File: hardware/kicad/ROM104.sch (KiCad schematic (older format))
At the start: 43 parts, among them J1 Screw_Terminal_01x06, J2 Screw_Terminal_01x06, J3 Screw_Terminal_01x06, J4 CAN, K1 SPDT_RELAY, K2 SPDT_RELAY, K3 SPDT_RELAY, K4 SPDT_RELAY, K5 SPDT_RELAY, K6 SPDT_RELAY, SW1 HEX_ENCODER, SW2 BUS, SW3 HEX_ENCODER, U1 L293D, U2 74HC595, U3 L293D, U4 L293D, U5 MCP2551-I-P, U6 TMR_2411, U7 Teensy_3.2

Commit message: New PCB layout
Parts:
- removed D1, D2, D3, D4, D5, D6, D7, D8: D_Small, Diode_THT:D_DO-34_SOD68_P2.54mm_Vertical_AnodeUp, symbol Device:D_Small
- removed SW1, SW3: HEX_ENCODER, PDJR-connectors:FR01-SR16P-ST, symbol pdjr:HEX_ENCODER
- added C1: 100n, Capacitor_THT:C_Rect_L4.6mm_W3.0mm_P2.50mm_MKS02_FKP02, symbol Device:C
- added SW1: INSTANCE, Package_DIP:DIP-16_W7.62mm, symbol Switch:SW_DIP_x08
- renumbered D9 to D1, D10 to D2, D11 to D3, D12 to D4, D13 to D5, D14 to D6, D15 to D7, D16 to D8, U3 to U2, U2 to U3
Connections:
- net labels added: ADDR_4, ADDR_5, ADDR_6, ADDR_7
- net labels removed: ADDR_HI, ADDR_LO
- no-connect marks 13 -> 11
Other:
- moved on the sheet: D1, D2, D3, D4, D5, D6, D7, D8, RN1, SW2, U3

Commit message: Add PRG switch
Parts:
- added SW3: PRG, Button_Switch_THT:SW_PUSH_6mm, symbol Switch:SW_Push
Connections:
- net labels added: PRG
- wire segments 290 -> 292
- no-connect marks 11 -> 10
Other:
- moved on the sheet: SW1, SW2
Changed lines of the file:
@@
 L power:GND #PWR02
 U 1 1 6084E21C
-P 1100 2450
-F 0 "#PWR02" H 1100 2200 50  0001 C CNN
-F 1 "GND" H 1105 2277 50  0000 C CNN
-F 2 "" H 1100 2450 50  0001 C CNN
-F 3 "" H 1100 2450 50  0001 C CNN
-	1    1100 2450
+P 750 2750
+F 0 "#PWR02" H 750 2500 50  0001 C CNN
+F 1 "GND" H 755 2577 50  0000 C CNN
+F 2 "" H 750 2750 50  0001 C CNN
+F 3 "" H 750 2750 50  0001 C CNN
+	1    750  2750
 	1    0    0    -1
 $EndComp
@@
 Wire Wire Line
 	8900 2350 9300 2350
-Text Label 1100 2250 2    50   ~ 0
+Text Label 1100 1950 2    50   ~ 0
 TERM_A
-Text Label 1700 2250 0    50   ~ 0
+Text Label 1700 1950 0    50   ~ 0
 TERM_B
 $Comp
@@
 	0    1    1    0
 $EndComp
-Text Label 1700 2350 0    50   ~ 0
+Text Label 1700 2050 0    50   ~ 0
 CAN_SCR
 $Comp
 L Switch:SW_DIP_x02 SW2
 U 1 1 62A67242
-P 1400 2250
-F 0 "SW2" H 1400 2500 50  0000 C CNN
-F 1 "BUS" H 1400 2100 50  0000 C CNN
-F 2 "Package_DIP:DIP-4_W7.62mm_LongPads" H 1400 2250 50  0001 C CNN
-F 3 "~" H 1400 2250 50  0001 C CNN
-	1    1400 2250
+P 1400 1950
+F 0 "SW2" H 1400 2200 50  0000 C CNN
+F 1 "BUS" H 1400 1800 50  0000 C CNN
+F 2 "Package_DIP:DIP-4_W7.62mm_LongPads" H 1400 1950 50  0001 C CNN
+F 3 "~" H 1400 1950 50  0001 C CNN
+	1    1400 1950
 	1    0    0    1
 $EndComp
@@
 Wire Wire Line
 	6750 5650 6750 5350
-Wire Wire Line
-	1100 2350 1100 2450
 $Comp
 L Device:LED D3
@@
 L Switch:SW_DIP_x08 SW1
 U 1 1 633236F9
-P 1400 1500
-F 0 "SW1" H 1400 1050 50  0000 C CNN
-F 1 "INSTANCE" H 1400 2076 50  0000 C CNN
-F 2 "Package_DIP:DIP-16_W7.62mm" H 1400 1500 50  0001 C CNN
-F 3 "~" H 1400 1500 50  0001 C CNN
-	1    1400 1500
+P 1400 1200
+F 0 "SW1" H 1400 750 50  0000 C CNN
+F 1 "INSTANCE" H 1400 1776 50  0000 C CNN
+F 2 "Package_DIP:DIP-16_W7.62mm" H 1400 1200 50  0001 C CNN
+F 3 "~" H 1400 1200 50  0001 C CNN
+	1    1400 1200
 	-1   0    0    -1
 $EndComp
 Wire Wire Line
+	1100 800  750  800
+Wire Wire Line
+	750  800  750  900
+Wire Wire Line
+	750  2050 1100 2050
+Wire Wire Line
+	1100 900  750  900
+Connection ~ 750  900
+Wire Wire Line
+	750  900  750  1000
+Wire Wire Line
+	1100 1000 750  1000
+Connection ~ 750  1000
+Wire Wire Line
+	750  1000 750  1100
+Wire Wire Line
 	1100 1100 750  1100
+Connection ~ 750  1100
 Wire Wire Line
 	750  1100 750  1200
-Wire Wire Line
-	750  2350 1100 2350
-Connection ~ 1100 2350
 Wire Wire Line
 	1100 1200 750  1200
@@
 Wire Wire Line
 	1100 1500 750  1500
-Connection ~ 750  1500
-Wire Wire Line
-	750  1500 750  1600
-Wire Wire Line
-	1100 1600 750  1600
-Connection ~ 750  1600
-Wire Wire Line
-	750  1600 750  1700
-Wire Wire Line
-	1100 1700 750  1700
-Connection ~ 750  1700
-Wire Wire Line
-	750  1700 750  1800
-Wire Wire Line
-	1100 1800 750  1800
-Wire Wire Line
-	750  1800 750  2350
+Wire Wire Line
+	750  1500 750  2050
+Text Label 1700 800  0    50   ~ 0
+ADDR_0
+Text Label 1700 900  0    50   ~ 0
+ADDR_1
+Text Label 1700 1000 0    50   ~ 0
+ADDR_2
 Text Label 1700 1100 0    50   ~ 0
-ADDR_0
+ADDR_3
 Text Label 1700 1200 0    50   ~ 0
-ADDR_1
+ADDR_4
 Text Label 1700 1300 0    50   ~ 0
-ADDR_2
+ADDR_5
 Text Label 1700 1400 0    50   ~ 0
-ADDR_3
+ADDR_6
 Text Label 1700 1500 0    50   ~ 0
-ADDR_4
-Text Label 1700 1600 0    50   ~ 0
-ADDR_5
-Text Label 1700 1700 0    50   ~ 0
-ADDR_6
-Text Label 1700 1800 0    50   ~ 0
 ADDR_7
 $Comp
@@
 Text Label 9550 4850 0    50   ~ 0
 ADDR_7
-Connection ~ 750  1800
+Connection ~ 750  1500
 $Comp
 L Device:C C1
@@
 	5750 800  5750 1100
 Connection ~ 5750 1100
-NoConn ~ 8450 4250
 NoConn ~ 8450 4350
+$Comp
+L Switch:SW_Push SW3
+U 1 1 633332C8
+P 1400 2650
+F 0 "SW3" H 1400 2550 50  0000 C CNN
+F 1 "PRG" H 1400 2844 50  0000 C CNN
+F 2 "Button_Switch_THT:SW_PUSH_6mm" H 1400 2850 50  0001 C CNN
+F 3 "~" H 1400 2850 50  0001 C CNN
+	1    1400 2650
+	1    0    0    -1
+$EndComp
+Wire Wire Line
+	750  2050 750  2650
+Wire Wire Line
+	750  2650 1200 2650
+Connection ~ 750  2050
+Wire Wire Line
+	750  2650 750  2750
+Connection ~ 750  2650
+Text Label 1600 2650 0    50   ~ 0
+PRG
+Text Label 8450 4250 2    50   ~ 0
+PRG
 $EndSCHEMATC

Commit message: PCB update
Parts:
- removed C1, C2: 100n, Capacitor_THT:C_Rect_L4.6mm_W3.0mm_P2.50mm_MKS02_FKP02, symbol Device:C
- removed C4: 100nF, Capacitor_THT:C_Rect_L4.6mm_W3.0mm_P2.50mm_MKS02_FKP02, symbol Device:C
- added C1, C10, C2, C3, C4, C5, C6, C7, C8: 100nF, Capacitor_THT:CP_Radial_D5.0mm_P2.00mm, symbol Device:CP_Small
- C9: renamed from C3; footprint Capacitor_THT:CP_Radial_D8.0mm_P5.00mm -> Capacitor_THT:CP_Radial_D10.0mm_P5.00mm
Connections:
- wire segments 292 -> 312
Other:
- moved on the sheet: J2, J3, K3, K4, K5, K6, U2, U4

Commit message: Revised PCB
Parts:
- removed C9: 1000uF, Capacitor_THT:CP_Radial_D10.0mm_P5.00mm, symbol Device:CP
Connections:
- wire segments 312 -> 308
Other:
- moved on the sheet: C1, C10, C2, C4, C5, C6, C7, J1, J2, J3, K1, K2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

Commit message: PCB update
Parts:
- SW3: footprint Button_Switch_THT:SW_PUSH_6mm -> PDJR-connectors:PCB_PUSH_BUTTON
- renumbered C8 to C1, C1 to C2, C2 to C3, C10 to C8, C3 to C9, J4 to J3, J3 to J4, U5 to U2, U6 to U3, U2 to U4, U4 to U5, U3 to U6
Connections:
- no-connect marks 10 -> 8
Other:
- note added: "CONFIGURATION"
- note added: "DISPLAY"
- note added: "POWER SUPPLY & CAN INTERFACE"
- note added: "RELAY OUTPUTS"
- note removed: "12/5 V DC-DC CONVERTER"
- note removed: "CAN INTERFACE"
- moved on the sheet: C1, C2, C3, C4, C5, C6, C7, C8, C9, D1, D2, D3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

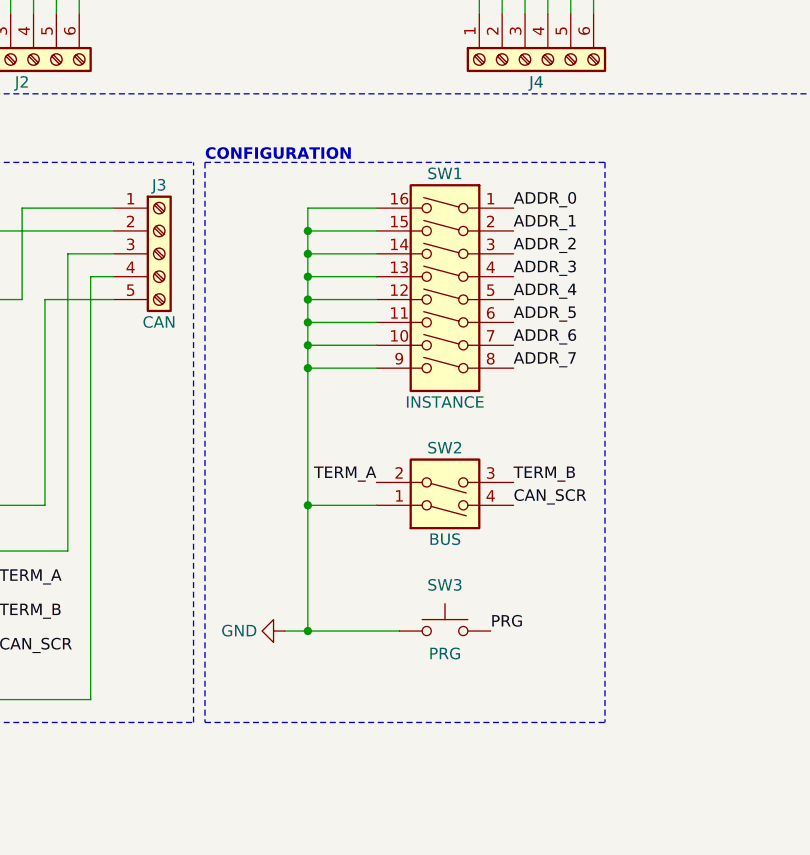
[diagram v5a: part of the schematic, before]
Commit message: Add PRG debounce
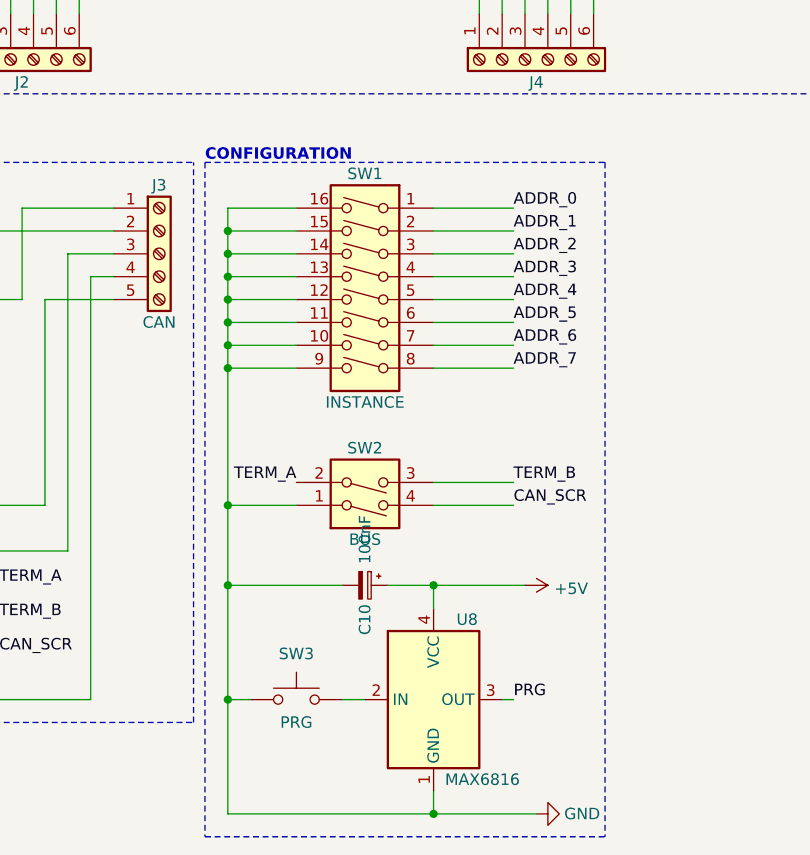
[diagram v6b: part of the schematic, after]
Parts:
- added C10: 100nF, Capacitor_THT:CP_Radial_D5.0mm_P2.00mm, symbol Device:CP_Small
- added U8: MAX6816, Package_TO_SOT_SMD:SOT-143, symbol Interface:MAX6816
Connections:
- net +5V: now also C10.1, U8.4 (VCC)
- net GND: now also C10.2, U8.1 (GND)
- net PRG: now also U8.3 (OUT); no longer SW3.2
- new net: SW3.2, U8.2 (IN)
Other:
- moved on the sheet: SW1, SW2, SW3
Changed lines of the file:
@@
 	3950 7000 4650 7000
-$Comp
-L power:GND #PWR011
-U 1 1 6084E21C
-P 5500 6700
-F 0 "#PWR011" H 5500 6450 50  0001 C CNN
-F 1 "GND" V 5500 6500 50  0000 C CNN
-F 2 "" H 5500 6700 50  0001 C CNN
-F 3 "" H 5500 6700 50  0001 C CNN
-	1    5500 6700
-	0    1    1    0
-$EndComp
 $Comp
 L power:GND #PWR017
@@
 Wire Wire Line
 	2900 6350 3300 6350
-Text Label 5900 6050 2    50   ~ 0
+Text Label 5550 6050 2    50   ~ 0
 TERM_A
 Text Label 6500 6050 0    50   ~ 0
@@
 L Switch:SW_DIP_x02 SW2
 U 1 1 62A67242
-P 6200 6050
-F 0 "SW2" H 6200 5900 50  0000 C CNN
-F 1 "BUS" H 6200 6300 50  0000 C CNN
-F 2 "Package_DIP:DIP-4_W7.62mm_LongPads" H 6200 6050 50  0001 C CNN
-F 3 "~" H 6200 6050 50  0001 C CNN
-	1    6200 6050
+P 5850 6050
+F 0 "SW2" H 5850 5900 50  0000 C CNN
+F 1 "BUS" H 5850 6300 50  0000 C CNN
+F 2 "Package_DIP:DIP-4_W7.62mm_LongPads" H 5850 6050 50  0001 C CNN
+F 3 "~" H 5850 6050 50  0001 C CNN
+	1    5850 6050
 	1    0    0    1
 $EndComp
@@
 L Switch:SW_DIP_x08 SW1
 U 1 1 633236F9
-P 6200 5250
-F 0 "SW1" H 6200 5800 50  0000 C CNN
-F 1 "INSTANCE" H 6200 4800 50  0000 C CNN
-F 2 "Package_DIP:DIP-16_W7.62mm" H 6200 5250 50  0001 C CNN
-F 3 "~" H 6200 5250 50  0001 C CNN
-	1    6200 5250
+P 5850 5250
+F 0 "SW1" H 5850 5800 50  0000 C CNN
+F 1 "INSTANCE" H 5850 4800 50  0000 C CNN
+F 2 "Package_DIP:DIP-16_W7.62mm" H 5850 5250 50  0001 C CNN
+F 3 "~" H 5850 5250 50  0001 C CNN
+	1    5850 5250
 	-1   0    0    -1
 $EndComp
 Wire Wire Line
-	5600 4850 5600 4950
-Wire Wire Line
-	5600 6150 5900 6150
-Connection ~ 5600 4950
-Wire Wire Line
-	5600 4950 5600 5050
-Connection ~ 5600 5050
-Wire Wire Line
-	5600 5050 5600 5150
-Connection ~ 5600 5150
-Wire Wire Line
-	5600 5150 5600 5250
-Connection ~ 5600 5250
-Wire Wire Line
-	5600 5250 5600 5350
-Connection ~ 5600 5350
-Wire Wire Line
-	5600 5350 5600 5450
-Connection ~ 5600 5450
-Wire Wire Line
-	5600 5450 5600 5550
-Wire Wire Line
-	5600 5550 5600 6150
+	5250 4850 5250 4950
+Wire Wire Line
+	5250 6150 5550 6150
+Connection ~ 5250 4950
+Wire Wire Line
+	5250 4950 5250 5050
+Connection ~ 5250 5050
+Wire Wire Line
+	5250 5050 5250 5150
+Connection ~ 5250 5150
+Wire Wire Line
+	5250 5150 5250 5250
+Connection ~ 5250 5250
+Wire Wire Line
+	5250 5250 5250 5350
+Connection ~ 5250 5350
+Wire Wire Line
+	5250 5350 5250 5450
+Connection ~ 5250 5450
+Wire Wire Line
+	5250 5450 5250 5550
+Wire Wire Line
+	5250 5550 5250 6150
 Text Label 6500 4850 0    50   ~ 0
 ADDR_0
@@
 L Switch:SW_Push SW3
 U 1 1 633332C8
-P 6200 6700
-F 0 "SW3" H 6200 6900 50  0000 C CNN
-F 1 "PRG" H 6200 6600 50  0000 C CNN
-F 2 "PDJR-connectors:PCB_PUSH_BUTTON" H 6200 6900 50  0001 C CNN
-F 3 "~" H 6200 6900 50  0001 C CNN
-	1    6200 6700
-	1    0    0    -1
-$EndComp
-Wire Wire Line
-	5600 6150 5600 6700
-Wire Wire Line
-	5600 6700 6000 6700
-Text Label 6400 6700 0    50   ~ 0
+P 5550 7000
+F 0 "SW3" H 5550 7200 50  0000 C CNN
+F 1 "PRG" H 5550 6900 50  0000 C CNN
+F 2 "PDJR-connectors:PCB_PUSH_BUTTON" H 5550 7200 50  0001 C CNN
+F 3 "~" H 5550 7200 50  0001 C CNN
+	1    5550 7000
+	1    0    0    -1
+$EndComp
+Wire Wire Line
+	5250 6150 5250 6500
+Text Label 6500 7000 0    50   ~ 0
 PRG
 Text Label 9100 1950 2    50   ~ 0
@@
 	0    1    1    0
 $EndComp
-Connection ~ 5600 6700
-Wire Wire Line
-	5600 6700 5500 6700
 Wire Notes Line
 	5150 4650 6900 4650
@@
 	700  7100 5100 7100
 Wire Notes Line
-	5150 7100 6900 7100
-Wire Notes Line
-	6900 4650 6900 7100
-Wire Notes Line
-	5150 4650 5150 7100
-Connection ~ 5600 5550
-Connection ~ 5600 6150
-Wire Wire Line
-	5900 4850 5600 4850
-Wire Wire Line
-	5900 4950 5600 4950
-Wire Wire Line
-	5900 5050 5600 5050
-Wire Wire Line
-	5900 5150 5600 5150
-Wire Wire Line
-	5900 5250 5600 5250
-Wire Wire Line
-	5900 5350 5600 5350
-Wire Wire Line
-	5900 5450 5600 5450
-Wire Wire Line
-	5900 5550 5600 5550
+	5150 7600 6900 7600
+Wire Notes Line
+	6900 4650 6900 7600
+Wire Notes Line
+	5150 4650 5150 7600
+Connection ~ 5250 5550
+Wire Wire Line
+	5550 4850 5250 4850
+Wire Wire Line
+	5550 4950 5250 4950
+Wire Wire Line
+	5550 5050 5250 5050
+Wire Wire Line
+	5550 5150 5250 5150
+Wire Wire Line
+	5550 5250 5250 5250
+Wire Wire Line
+	5550 5350 5250 5350
+Wire Wire Line
+	5550 5450 5250 5450
+Wire Wire Line
+	5550 5550 5250 5550
+$Comp
+L Interface:MAX6816 U8
+U 1 1 6336163A
+P 6150 7000
+F 0 "U8" H 6250 7350 50  0000 L CNN
+F 1 "MAX6816" H 6200 6650 50  0000 L CNN
+F 2 "Package_TO_SOT_SMD:SOT-143" H 6800 6550 50  0001 C CNN
+F 3 "https://datasheets.maximintegrated.com/en/ds/1896.pdf" H 6150 7000 50  0001 C CNN
+	1    6150 7000
+	1    0    0    -1
+$EndComp
+Wire Wire Line
+	6150 7400 6150 7500
+Wire Wire Line
+	5850 7000 5750 7000
+Wire Wire Line
+	6150 6600 6150 6500
+Wire Wire Line
+	6150 6500 6550 6500
+$Comp
+L Device:CP_Small C10
+U 1 1 6355CB0C
+P 5850 6500
+F 0 "C10" H 6000 6500 50  0000 C CNN
+F 1 "100nF" H 5650 6500 50  0000 C CNN
+F 2 "Capacitor_THT:CP_Radial_D5.0mm_P2.00mm" H 5850 6500 50  0001 C CNN
+F 3 "~" H 5850 6500 50  0001 C CNN
+	1    5850 6500
+	0    1    1    0
+$EndComp
+Wire Wire Line
+	5750 6500 5250 6500
+Connection ~ 5250 6500
+Connection ~ 5250 6150
+Wire Wire Line
+	5950 6500 6150 6500
+Connection ~ 6150 6500
+Wire Wire Line
+	6450 7000 6500 7000
+Wire Wire Line
+	6150 7500 5250 7500
+Wire Wire Line
+	5250 6500 5250 7000
+Wire Wire Line
+	5350 7000 5250 7000
+Connection ~ 5250 7000
+Wire Wire Line
+	5250 7000 5250 7500
+$Comp
+L power:+5V #PWR011
+U 1 1 6369DCBF
+P 6550 6500
+F 0 "#PWR011" H 6550 6350 50  0001 C CNN
+F 1 "+5V" V 6565 6628 50  0000 L CNN
+F 2 "" H 6550 6500 50  0001 C CNN
+F 3 "" H 6550 6500 50  0001 C CNN
+	1    6550 6500
+	0    1    1    0
+$EndComp
+$Comp
+L power:GND #PWR020
+U 1 1 63724529
+P 6600 7500
+F 0 "#PWR020" H 6600 7250 50  0001 C CNN
+F 1 "GND" V 6600 7300 50  0000 C CNN
+F 2 "" H 6600 7500 50  0001 C CNN
+F 3 "" H 6600 7500 50  0001 C CNN
+	1    6600 7500
+	0    -1   -1   0
+$EndComp
+Wire Wire Line
+	6600 7500 6150 7500
+Connection ~ 6150 7500
+Wire Wire Line
+	6150 4850 6500 4850
+Wire Wire Line
+	6150 4950 6500 4950
+Wire Wire Line
+	6150 5050 6500 5050
+Wire Wire Line
+	6150 5150 6500 5150
+Wire Wire Line
+	6150 5250 6500 5250
+Wire Wire Line
+	6150 5350 6500 5350
+Wire Wire Line
+	6150 5450 6500 5450
+Wire Wire Line
+	6150 5550 6500 5550
+Wire Wire Line
+	6150 6050 6500 6050
+Wire Wire Line
+	6150 6150 6500 6150
 $EndSCHEMATC

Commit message: Tweaks
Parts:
- K1, K2, K3, K4, K5, K6: symbol pdjr:SPDT_RELAY -> ROM104-rescue:SPDT_RELAY-pdjr
- U3: symbol pdjr:TMR_2411 -> ROM104-rescue:TMR_2411-pdjr
- U7: symbol pdjr:Teensy_3.2 -> ROM104-rescue:Teensy_3.2-pdjr
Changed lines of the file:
@@
 NoConn ~ 9100 1850
 $Comp
-L pdjr:TMR_2411 U3
+L ROM104-rescue:TMR_2411-pdjr U3
 U 1 1 6327DB22
 P 2950 5050
@@
 ADDR_7
 $Comp
-L pdjr:Teensy_3.2 U7
+L ROM104-rescue:Teensy_3.2-pdjr U7
 U 1 1 60F2AB82
 P 10200 3150
@@
 	7050 2700 7300 2700
 $Comp
-L pdjr:SPDT_RELAY K6
+L ROM104-rescue:SPDT_RELAY-pdjr K6
 U 1 1 637805D9
 P 6950 3200
@@
 $EndComp
 $Comp
-L pdjr:SPDT_RELAY K5
+L ROM104-rescue:SPDT_RELAY-pdjr K5
 U 1 1 637805CC
 P 6100 3200
@@
 	5000 3000 5050 3000
 $Comp
-L pdjr:SPDT_RELAY K4
+L ROM104-rescue:SPDT_RELAY-pdjr K4
 U 1 1 63768F03
 P 4700 3200
@@
 $EndComp
 $Comp
-L pdjr:SPDT_RELAY K3
+L ROM104-rescue:SPDT_RELAY-pdjr K3
 U 1 1 63768EF6
 P 3850 3200
@@
 	2750 3000 2800 3000
 $Comp
-L pdjr:SPDT_RELAY K2
+L ROM104-rescue:SPDT_RELAY-pdjr K2
 U 1 1 632D0338
 P 2450 3200
@@
 $EndComp
 $Comp
-L pdjr:SPDT_RELAY K1
+L ROM104-rescue:SPDT_RELAY-pdjr K1
 U 1 1 632C2C12
 P 1600 3200

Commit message: Tweaks
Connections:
- net CH0_EN is gone; now on net CH1_EN: U1.9 (EN3,4), U7.23 (D21)
- net CH1_EN: no longer U1.1 (EN1,2), U7.22 (D20)
- net CH2_EN: now also U1.1 (EN1,2), U7.22 (D20); no longer U4.9 (EN3,4), U7.21 (D19)
- net CH3_EN: now also U4.9 (EN3,4), U7.21 (D19); no longer U4.1 (EN1,2), U7.20 (D18)
- net CH4_EN: now also U4.1 (EN1,2), U7.20 (D18); no longer U5.9 (EN3,4), U7.19 (D17)
- net CH5_EN: now also U5.9 (EN3,4), U7.19 (D17); no longer U5.1 (EN1,2), U7.18 (D16)
- new net CH6_EN: U5.1 (EN1,2), U7.18 (D16)
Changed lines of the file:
@@
 	-1   0    0    1
 $EndComp
-Text Label 9100 2350 2    50   ~ 0
+Text Label 9100 2450 2    50   ~ 0
 CH3_EN
-Text Label 9100 2450 2    50   ~ 0
+Text Label 9100 2550 2    50   ~ 0
 CH2_EN
-Text Label 9100 2550 2    50   ~ 0
+Text Label 9100 2650 2    50   ~ 0
 CH1_EN
-Text Label 9100 2650 2    50   ~ 0
-CH0_EN
+Text Label 9100 2150 2    50   ~ 0
+CH6_EN
 Text Label 9100 2750 2    50   ~ 0
 SET
@@
 Wire Wire Line
 	4450 5250 4450 6150
+Text Label 9100 2350 2    50   ~ 0
+CH4_EN
 Text Label 9100 2250 2    50   ~ 0
-CH4_EN
-Text Label 9100 2150 2    50   ~ 0
 CH5_EN
 $Comp
@@
 Wire Wire Line
 	6250 1600 6250 1500
+Text Label 1050 1000 2    50   ~ 0
+CH4_EN
 Text Label 1050 900  2    50   ~ 0
-CH4_EN
-Text Label 1050 800  2    50   ~ 0
 CH5_EN
 Wire Wire Line
@@
 Wire Wire Line
 	4000 1600 4000 1500
+Text Label 1050 1200 2    50   ~ 0
+CH2_EN
 Text Label 1050 1100 2    50   ~ 0
-CH2_EN
-Text Label 1050 1000 2    50   ~ 0
 CH3_EN
 Wire Wire Line
@@
 Wire Wire Line
 	1750 1600 1750 1500
+Text Label 1050 800  2    50   ~ 0
+CH6_EN
 Text Label 1050 1300 2    50   ~ 0
-CH0_EN
-Text Label 1050 1200 2    50   ~ 0
 CH1_EN
 $Comp
